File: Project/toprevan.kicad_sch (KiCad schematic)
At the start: 29 parts, among them J1 JST SH, J2 Pico EZmate, J3 USB_C_Receptacle_USB2.0, J4 ARGB, SW1 BOOT0, U1 STM32F401CBUx, U3 XC6206PxxxMR, Y1 8 MHz

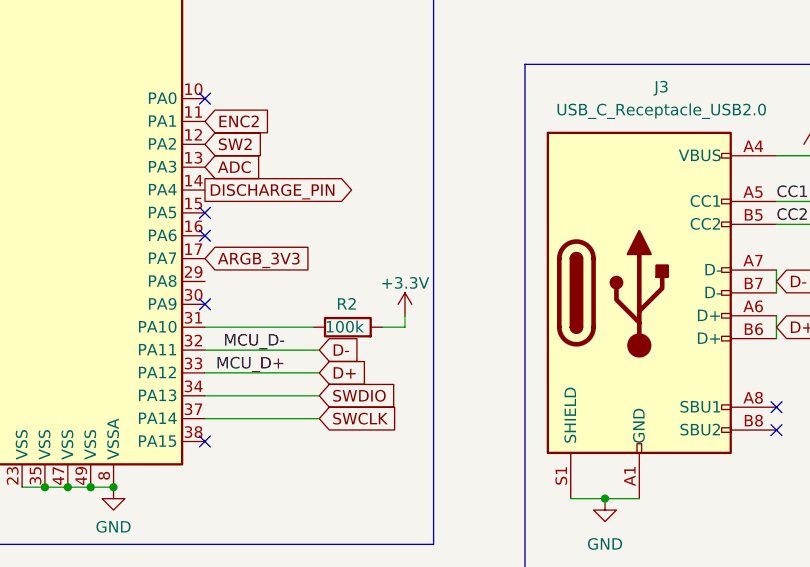
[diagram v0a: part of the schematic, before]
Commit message: pcb & plate revision
move mux, add cutout for all plates for boot
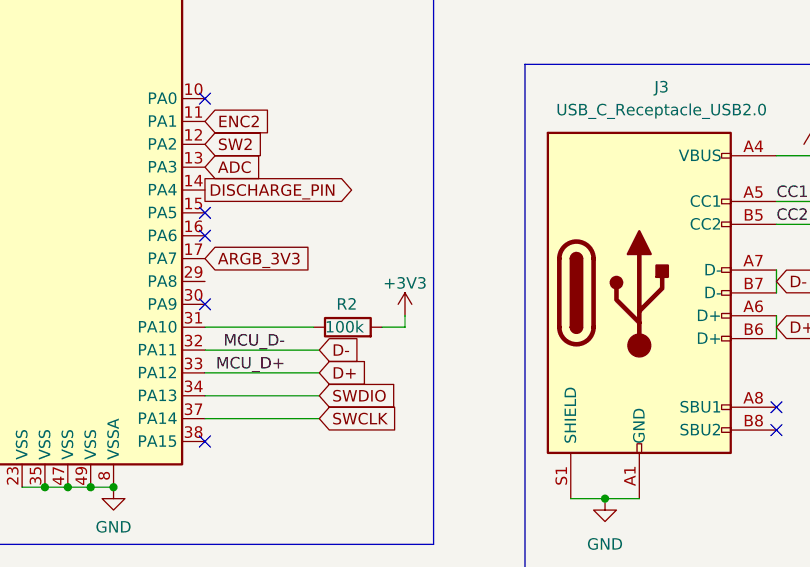
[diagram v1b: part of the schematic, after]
